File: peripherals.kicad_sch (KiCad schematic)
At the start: 73 parts, among them J401 JTAG, J402 USB_B_Micro, J403 Conn_02x20, J404 Micro_SD_Card_Det2, J405 USB1, J406 USB2, U401 FT230XQ, U402 MT48LC16M16A2, U403 MX25L1606, U404 TPD4E02B04DQA, U405 AP3417C, U406 AP3417C, U407 AP3417C, X401 XO32

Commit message: Cosmetics
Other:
- note added: "CMOS Serial Flash (16Mb)"
- note added: "Clock (100MHz)"
- note added: "DC/DC Converters. Provide +1.1V, +2.5V, +3.3V"
- note added: "External SDRAM (256Mb)"
- note added: "GPIO Breakout"
- note added: "Host USB ports"
- note added: "JTAG Connector"
- note added: "USB/Serial"
- note added: "microSD Card Socket"
- note removed: "CLOCK"
- note removed: "USB SERIAL/JTAG"
- moved on the sheet: C401, C402, C403, C404, C405, C406, C407, C408, C409, C410, C411, C412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

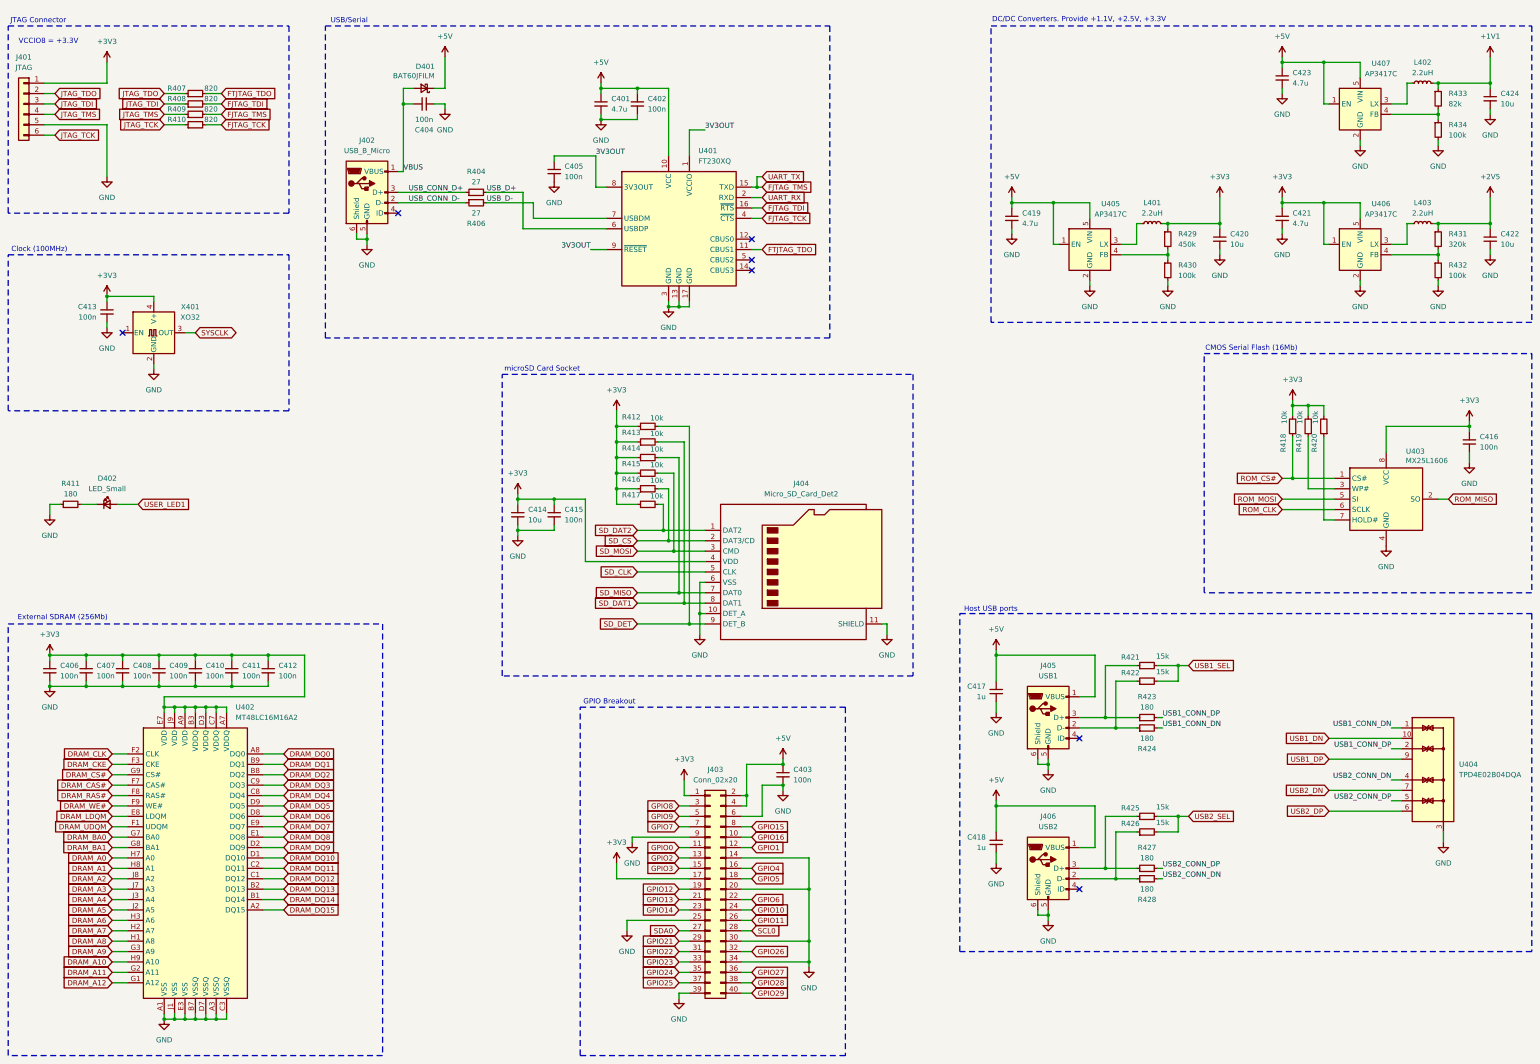
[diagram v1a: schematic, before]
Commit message: Towards routing RAM
 - Moved the RAM to its own sheet
 - Use the ECP5 prefix to capture impedance controlled traces
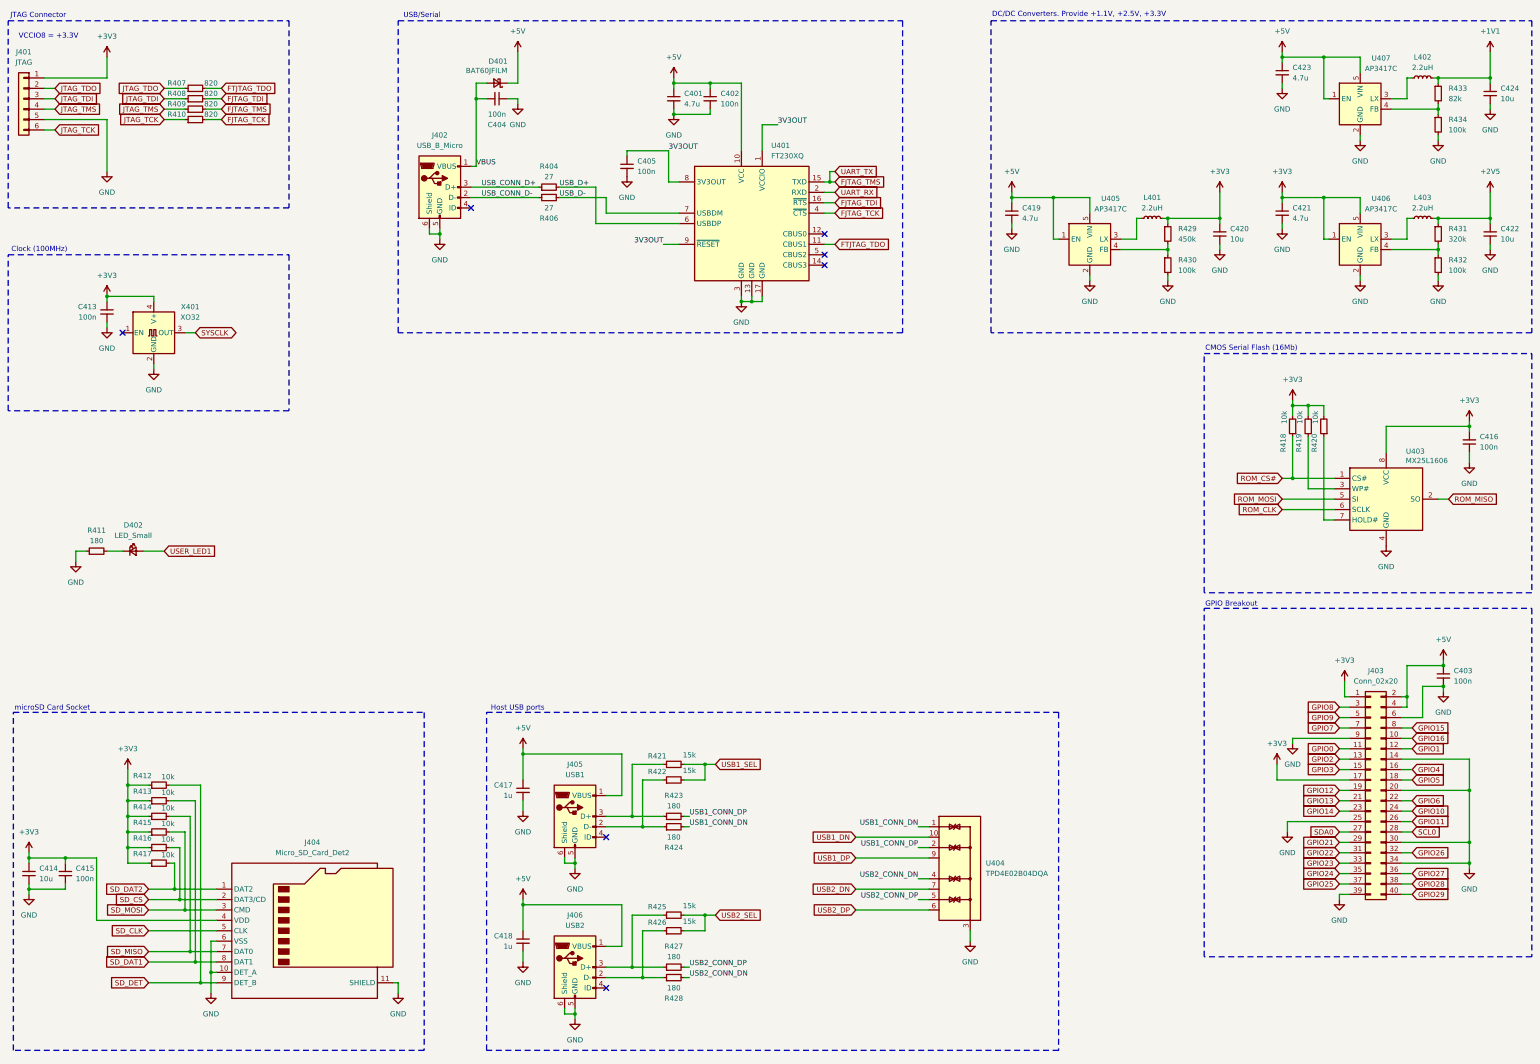
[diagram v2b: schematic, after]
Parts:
- removed C406, C407, C408, C409, C410, C411, C412: 100n, Capacitor_SMD:C_0201_0603Metric, symbol Device:C_Small
- removed U402: MT48LC16M16A2, Package_BGA_Extra:Micron_VFBGA-64_8.0x8.0mm_Layout9x9_P0.8mm, symbol Memory_RAM_Extra:MT48LC16M16A2
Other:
- note removed: "External SDRAM (256Mb)"
- moved on the sheet: C401, C402, C403, C404, C405, C414, C415, C417, C418, C419, C420, C421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

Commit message: First whole routing
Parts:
- removed C420, C422, C424: 10u, Capacitor_SMD:C_0603_1608Metric, symbol Device:C_Small
- removed C421, C423: 4.7u, Capacitor_SMD:C_0603_1608Metric, symbol Device:C_Small
- removed J401: JTAG, Connector_PinHeader_2.00mm:PinHeader_1x06_P2.00mm_Vertical, symbol Connector_Generic:Conn_01x06
- removed J406: USB2, Connector_USB:USB_Micro-B_Amphenol_10118193-0001LF_Horizontal, symbol Connector:USB_B_Micro
- removed R431: 320k, Resistor_SMD:R_0402_1005Metric, symbol Device:R_Small
- removed R432, R434: 100k, Resistor_SMD:R_0402_1005Metric, symbol Device:R_Small
- removed R433: 82k, Resistor_SMD:R_0402_1005Metric, symbol Device:R_Small
- removed U404: TPD4E02B04DQA, Package_SON:USON-10_2.5x1.0mm_P0.5mm, symbol Power_Protection:TPD4E02B04DQA
- removed U405, U406, U407: AP3417C, Package_TO_SOT_SMD:SOT-23-5, symbol Regulator_Switching_Extra:AP3417C
- added C406, C408, C410: 4.7uF, Capacitor_SMD:C_0603_1608Metric, symbol Device:C_Small
- added C407, C409, C412: 22uF, Capacitor_SMD:C_0603_1608Metric, symbol Device:C_Small
- added C411: 10uF, Capacitor_SMD:C_0603_1608Metric, symbol Device:C_Small
- added D403: LED_Small, LED_SMD:LED_0603_1608Metric, symbol Device:LED_Small
- added R401: 200k, Resistor_SMD:R_0402_1005Metric, symbol Device:R_Small
- added R402, R405: 100k, Resistor_SMD:R_0402_1005Metric, symbol Device:R_Small
- added R403: 82.5k, Resistor_SMD:R_0402_1005Metric, symbol Device:R_Small
- added U1: TPD2EUSB30, Package_TO_SOT_SMD:Texas_DRT-3, symbol Power_Protection:TPD2EUSB30
- added U402, U404, U405: TLV62569DRL, Package_TO_SOT_SMD:SOT-563, symbol Regulator_Switching:TLV62569DRL
- added U406: TLV75801PDRV, Package_SON:WSON-6-1EP_2x2mm_P0.65mm_EP1x1.6mm, symbol Regulator_Linear:TLV75801PDRV
- C403: footprint Capacitor_SMD:C_0201_0603Metric -> Capacitor_SMD:C_0603_1608Metric; MPN (none) -> C14663
- C404, C413: MPN (none) -> C1525
- C417: footprint Capacitor_SMD:C_0402_1005Metric -> Capacitor_SMD:C_0603_1608Metric
- C418: value 1u -> 1uF; MPN (none) -> C52923
- C419: value 4.7u -> 1uF; footprint Capacitor_SMD:C_0603_1608Metric -> Capacitor_SMD:C_0402_1005Metric; MPN (none) -> C52923
- D401: MFN C133103 -> (none); MPN (none) -> C133103
- D402: MPN (none) -> C2286
- J402, J405: MFN C132562 -> (none); MPN (none) -> C132562
- J404: MFN C585350 -> (none); MPN (none) -> C585350
- L401, L402, L403: footprint Inductor_SMD:L_0603_1608Metric -> Inductor_SMD:L_0805_2012Metric; MFN C365953 -> (none); MPN (none) -> C383369
- R407: value 820 -> 450k; MPN (none) -> C5159688
- R408, R410: value 820 -> 100k; MPN (none) -> C25741
- R409: value 820 -> 330k; footprint Resistor_SMD:R_0402_1005Metric -> Resistor_SMD:R_0603_1608Metric; MPN (none) -> C23137
- R412, R413, R414, R415, R416, R417, R418, R419, R420: MPN (none) -> C25744
- R421, R422: MPN (none) -> C25756
- R425: value 15k -> 22k; MPN (none) -> C25768
- R426: value 15k -> 10k; MPN (none) -> C25744
- R427, R428: value 180 -> 10k; MPN (none) -> C25744
- R429: value 450k -> 10k; MPN (none) -> C25744
- R430: value 100k -> 180
- U401: MFN C128629 -> (none); MPN (none) -> C128629
- U403: footprint Package_SON:WSON-8-1EP_6x5mm_P1.27mm_EP3.4x4mm -> Package_SO_Extra:SOP-8-1EP_3.9x4.9mm_P1.27m_EP4.1x3.5mm; MPN (none) -> C3014050
- X401: MFN C4353707 -> (none); MPN (none) -> C4353707
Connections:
- net USB2_CONN_DN is gone; now on net GND: R428.2
- net USB2_CONN_DP is gone; now on net JTAG_TDI: R427.2
- net +1V1: now also C409.1, C412.1, R403.1
- net +2V5: now also C419.1, R409.1, U406.1 (OUT); no longer L403.2
- net +3V3: now also C418.1, L403.2, R407.1, R426.1, R427.1, C411.1, U406.4 (EN), U406.6 (IN); no longer L401.2
- net +5V: now also C406.1, C408.1, C410.1, U402.3 (VIN), U402.5 (EN), U404.3 (VIN), U404.5 (EN), U405.3 (VIN), U405.5 (EN); no longer C418.1, C419.1
- net GND: now also R408.2, R410.2, R430.1, C406.2, C407.2, C408.2, C409.2, C410.2, C411.2, C412.2, R402.2, R405.2, U1.3 (GND), U402.2 (GND), U404.2 (GND), U405.2 (GND), U406.3 (GND), U406.7 (GND); no longer R430.2
- net JTAG_TCK: now also R428.1, U401.4 (~{CTS}); no longer R410.1
- net JTAG_TDI: now also U401.16 (~{RTS}); no longer R408.1
- net JTAG_TDO: now also R426.2, U401.11 (CBUS1); no longer R407.1
- net JTAG_TMS: now also R429.2, U401.15 (TXD); no longer R409.1
- net USB1_CONN_DN: now also J405.2 (D-), R422.1, R424.1; no longer R424.2
- net USB1_CONN_DP: now also J405.3 (D+), R421.1, R423.1; no longer R423.2
- net USB1_DN: now also R424.2, U1.1 (D+)
- net USB1_DP: now also R423.2, U1.2 (D-)
- net at R425.1: now also R409.2; no longer R427.1
- net SW2: now reaches L402.1
- net SW2: now also U404.4 (SW)
- net SW3: now reaches L403.1
- net SW3: now also U405.4 (SW)
- net SW1: now reaches L401.1
- net SW1: now also U402.4 (SW)
- net ~{HOLD}: now reaches R420.1, U403.7 (HOLD#)
- net ~{WP}: now reaches R419.1, U403.3 (WP#)
- removed net FJTAG_TCK: R410.2, U401.4 (~{CTS})
- removed net FJTAG_TDI: R408.2, U401.16 (~{RTS})
- removed net FJTAG_TMS: R409.2, U401.15 (TXD)
- net FTJTAG_TDO renamed FB3
- net FB3: now also R408.1, U405.1 (FB); no longer U401.11 (CBUS1)
- net USB2_SEL renamed FB4
- net FB4: now also R410.1, U406.2 (FB); no longer R426.2
- new net: D403.1 (K), R430.2
- new net +1V8: C407.1, L401.2, R401.1
- new net FB1: R401.2, R402.1, U402.1 (FB)
- new net FB2: R403.2, R405.1, U404.1 (FB)
- new net USER_LED2: D403.2 (A)
- no-connect marks 7 -> 6
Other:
- note added: "Additional JTAG connector"
- note added: "DC/DC Converters. Provide +1.1V, +1.8V, +2.5V, +3.3V"
- note added: "User LEDs"
- note removed: "DC/DC Converters. Provide +1.1V, +2.5V, +3.3V"
- note removed: "JTAG Connector"
- note removed: "VCCIO8 = +3.3V"
- moved on the sheet: C413, C416, C417, J405, R418, R419, R420, R421, R422, R423, R424, U403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

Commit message: Update some component values and complete MPN for BOM
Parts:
- C401: value 4.7u -> 4.7uF; MPN (none) -> C19666
- C402, C405, C415, C416: value 100n -> 100nF; MPN (none) -> C190183
- C403, C404: value 100n -> 100nF
- C406, C408, C410: MPN (none) -> C19666
- C413: value 100n -> 100nF; MPN C1525 -> C190183
- C414: value 10u -> 10uF; MPN (none) -> C19702
- C417: value 1u -> 1uF; MPN (none) -> C15849
- D401: value BAT60JFILM -> 1N5819WS; MPN C133103 -> C191023
- J402: value USB_B_Micro -> Amph 10118193-0001LF
- J403: now not fitted
- J404: value Micro_SD_Card_Det2 -> Molex 1040310811
- J405: value USB1 -> Amph 10118193-0001LF
- R404, R406: MPN (none) -> C25100
- R411, R423, R424, R430: MPN (none) -> C138045
- U1: MPN (none) -> C97502
- U406: MPN (none) -> C2876308
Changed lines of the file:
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@@
 			)
 		)
+		(property "MPN" "C97502"
+			(at 248.92 231.14 0)
+			(effects
+				(font
+					(size 1.27 1.27)
+				)
+				(hide yes)
+			)
+		)
 		(pin "3"
 		)
@@
 			)
 		)
-		(property "Value" "USB_B_Micro"
+		(property "Value" "Amph 10118193-0001LF"
 			(at 130.81 53.34 0)
 			(effects
@@
 			)
 		)
-		(property "Value" "100n"
+		(property "Value" "100nF"
 			(at 179.07 59.6962 0)
 			(effects
@@
 			)
 		)
+		(property "MPN" "C190183"
+			(at 176.53 58.42 0)
+			(effects
+				(font
+					(size 1.27 1.27)
+				)
+				(hide yes)
+			)
+		)
 		(pin "2"
 		)
@@
 			)
 		)
-		(property "Value" "USB1"
+		(property "Value" "Amph 10118193-0001LF"
 			(at 170.18 226.06 0)
 			(effects
@@
 			)
 		)
+		(property "MPN" "C19666"
+			(at 283.21 90.17 0)
+			(effects
+				(font
+					(size 1.27 1.27)
+				)
+				(hide yes)
+			)
+		)
 		(pin "2"
 		)
@@
 			)
 		)
-		(property "Value" "10u"
+		(property "Value" "10uF"
 			(at 33.02 232.4162 0)
 			(effects
@@
 			)
 		)
+		(property "MPN" "C19702"
+			(at 30.48 231.14 0)
+			(effects
+				(font
+					(size 1.27 1.27)
+				)
+				(hide yes)
+			)
+		)
 		(pin "2"
 		)
@@
 			)
 		)
+		(property "MPN" "C25100"
+			(at 157.48 66.04 0)
+			(effects
+				(font
+					(size 1.27 1.27)
+				)
+				(hide yes)
+			)
+		)
 		(pin "1"
 		)
@@
 			)
 		)
+		(property "MPN" "C138045"
+			(at 207.01 236.22 0)
+			(effects
+				(font
+					(size 1.27 1.27)
+				)
+				(hide yes)
+			)
+		)
 		(pin "2"
 		)
@@
 			)
 		)
-		(property "Value" "100n"
+		(property "Value" "100nF"
 			(at 46.99 109.2262 0)
 			(effects
@@
 			)
 		)
-		(property "MPN" "C1525"
+		(property "MPN" "C190183"
 			(at 49.53 107.95 0)
 			(effects
@@
 			)
 		)
-		(property "Value" "Micro_SD_Card_Det2"
+		(property "Value" "Molex 1040310811"
 			(at 99.695 226.06 0)
 			(effects
@@
 			)
 		)
-		(property "Value" "BAT60JFILM"
+		(property "Value" "1N5819WS"
 			(at 142.24 35.052 0)
 			(effects
@@
 			)
 		)
-		(property "MPN" "C133103"
+		(property "MPN" "C191023"
 			(at 144.78 38.1 0)
 			(effects
@@
 			)
 		)
+		(property "MPN" "C138045"
+			(at 207.01 238.76 0)
+			(effects
+				(font
+					(size 1.27 1.27)
+				)
+				(hide yes)
+			)
+		)
 		(pin "2"
 		)
@@
 			)
 		)
-		(property "Value" "100n"
+		(property "Value" "100nF"
 			(at 199.39 43.1862 0)
 			(effects
@@
 			)
 		)
+		(property "MPN" "C190183"
+			(at 196.85 41.91 0)
+			(effects
+				(font
+					(size 1.27 1.27)
+				)
+				(hide yes)
+			)
+		)
 		(pin "2"
 		)
@@
 			)
 		)
-		(property "Value" "100n"
+		(property "Value" "100nF"
 			(at 41.91 232.4162 0)
 			(effects
@@
 			)
 		)
+		(property "MPN" "C190183"
+			(at 39.37 231.14 0)
+			(effects
+				(font
+					(size 1.27 1.27)
+				)
+				(hide yes)
+			)
+		)
 		(pin "2"
 		)
@@
 			)
 		)
+		(property "MPN" "C25100"
+			(at 157.48 63.5 0)
+			(effects
+				(font
+					(size 1.27 1.27)
+				)
+				(hide yes)
+			)
+		)
 		(pin "1"
 		)
@@
 			)
 		)
+		(property "MPN" "C138045"
+			(at 46.99 166.37 0)
+			(effects
+				(font
+					(size 1.27 1.27)
+				)
+				(hide yes)
+			)
+		)
 		(pin "2"
 		)
@@
 			)
 		)
+		(property "MPN" "C19666"
+			(at 283.21 121.92 0)
+			(effects
+				(font
+					(size 1.27 1.27)
+				)
+				(hide yes)
+			)
+		)
 		(pin "2"
 		)
@@
 			)
 		)
+		(property "MPN" "C138045"
+			(at 46.99 152.4 0)
+			(effects
+				(font
+					(size 1.27 1.27)
+				)
+				(hide yes)
+			)
+		)
 		(pin "2"
 		)
@@
 			)
 		)
-		(property "Value" "100n"
+		(property "Value" "100nF"
 			(at 378.46 184.1562 0)
 			(effects
@@
 			)
 		)
-		(property "Value" "100n"
+		(property "Value" "100nF"
 			(at 231.14 142.2335 0)
 			(effects
@@
 			)
 		)
+		(property "MPN" "C190183"
+			(at 228.6 140.97 0)
+			(effects
+				(font
+					(size 1.27 1.27)
+				)
+				(hide yes)
+			)
+		)
 		(pin "1"
 		)
@@
 		(in_bom yes)
 		(on_board yes)
-		(dnp no)
+		(dnp yes)
 		(fields_autoplaced yes)
 		(property "Reference" "J403"
@@
 			)
 		)
-		(property "Value" "1u"
+		(property "Value" "1uF"
 			(at 154.94 231.1462 0)
 			(effects
@@
 			)
 		)
+		(property "MPN" "C15849"
+			(at 157.48 229.87 0)
+			(effects
+				(font
+					(size 1.27 1.27)
+				)
+				(hide yes)
+			)
+		)
 		(pin "1"
 		)
@@
 			)
 		)
+		(property "MPN" "C19666"
+			(at 283.21 53.34 0)
+			(effects
+				(font
+					(size 1.27 1.27)
+				)
+				(hide yes)
+			)
+		)
 		(pin "2"
 		)
@@
 			)
 		)
+		(property "MPN" "C2876308"
+			(at 359.41 120.65 0)
+			(effects
+				(font
+					(size 1.27 1.27)
+				)
+				(hide yes)
+			)
+		)
 		(pin "3"
 		)
@@
 			)
 		)
-		(property "Value" "100n"
+		(property "Value" "100nF"
 			(at 144.7736 45.72 90)
 			(effects
@@
 			)
 		)
-		(property "Value" "4.7u"
+		(property "Value" "4.7uF"
 			(at 190.5 43.1862 0)
 			(effects
@@
 			(at 187.96 41.91 0)
 			(effects
+				(font
+					(size 1.27 1.27)
+				)
+				(hide yes)
+			)
+		)
+		(property "MPN" "C19666"
+			(at 187.96 41.91 0)
+			(effects

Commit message: Minor fixes
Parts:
- R426, R427, R428, R429: value 10k -> 4k7; MPN C25744 -> (none)
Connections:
- net UART_RX renamed UART_TX
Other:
- moved on the sheet: R426, R427, R428, R429
